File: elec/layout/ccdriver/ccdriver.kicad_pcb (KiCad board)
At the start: 2 copper layers, 25.4 x 14.8 mm, 31 parts, among them U1 ?, U2 ?, U3 ?, U4 ?, U5 ?, U6 ?, U7 ?

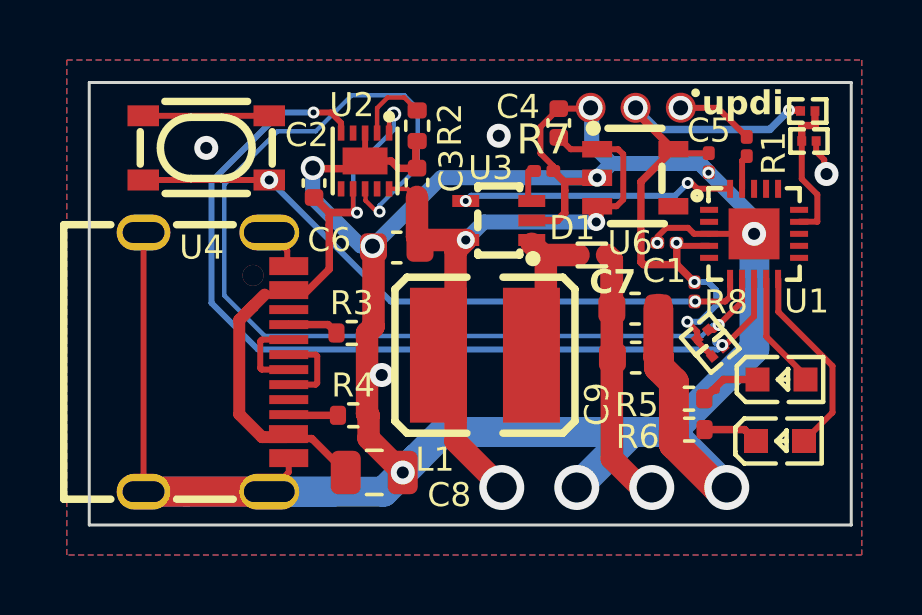
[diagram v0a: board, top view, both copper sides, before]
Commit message: fixed ground plane
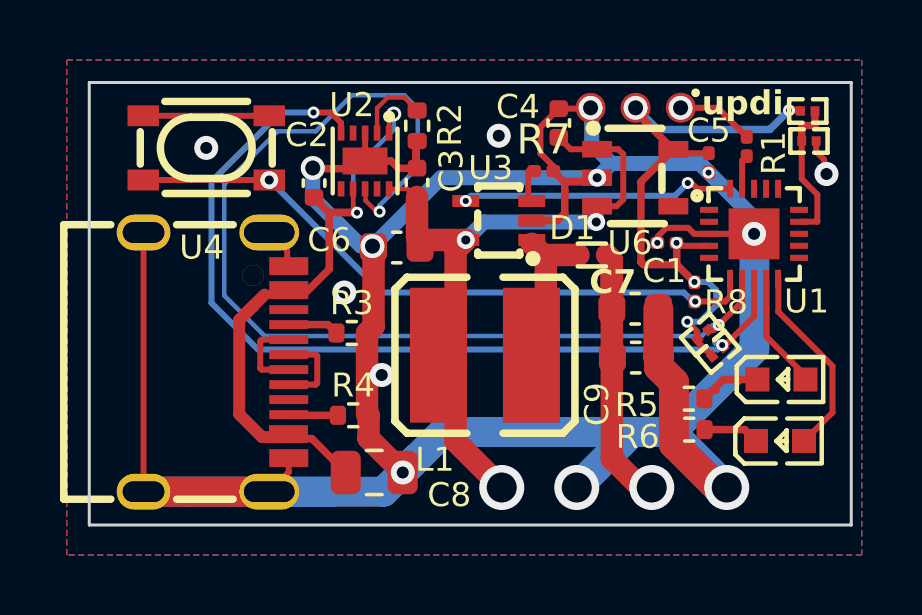
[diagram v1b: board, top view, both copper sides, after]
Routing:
- net gnd: vias 14 -> 15
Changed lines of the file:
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@@
 	)
 	(segment
-		(start 189.45 118.55)
-		(end 179.3 118.55)
+		(start 189.367893 118.55)
+		(end 189.067893 118.25)
 		(width 0.2)
 		(layer "B.Cu")
@@
 	)
 	(segment
-		(start 179.3 118.55)
+		(start 179 118.25)
 		(end 175.25 114.5)
+		(width 0.2)
+		(layer "B.Cu")
+		(net 33)
+	)
+	(segment
+		(start 189.067893 118.25)
+		(end 179 118.25)
+		(width 0.2)
+		(layer "B.Cu")
+		(net 33)
+	)
+	(segment
+		(start 189.45 118.55)
+		(end 189.367893 118.55)
 		(width 0.2)
 		(layer "B.Cu")
@@
 		(size 0.8)
 		(drill 0.4)
+		(layers "F.Cu" "B.Cu")
+		(net 36)
+	)
+	(via
+		(at 177.75 118.25)
+		(size 0.8)
+		(drill 0.4)

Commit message: fixed maybe
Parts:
- added ?: , , F.Cu at (174.7, 123.6)
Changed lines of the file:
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@@
 		)
 	)
+	(footprint ""
+		(layer "F.Cu")
+		(at 174.71 123.58)
+		(property "Reference" ""
+			(at 0 0 0)
+			(layer "F.SilkS")
+			(effects
+				(font
+					(size 1.27 1.27)
+					(thickness 0.15)
+				)
+			)
+		)
+		(property "Value" ""
+			(at 0 0 0)
+			(layer "F.Fab")
+			(effects
+				(font
+					(size 1.27 1.27)
+					(thickness 0.15)
+				)
+			)
+		)
+		(property "Footprint" ""
+			(at 0 0 0)
+			(layer "F.Fab")
+			(hide yes)
+			(effects
+				(font
+					(size 1.27 1.27)
+					(thickness 0.15)
+				)
+			)
+		)
+		(property "Datasheet" ""
+			(at 0 0 0)
+			(layer "F.Fab")
+			(hide yes)
+			(effects
+				(font
+					(size 1.27 1.27)
+					(thickness 0.15)
+				)
+			)
+		)
+		(property "Description" ""
+			(at 0 0 0)
+			(layer "F.Fab")
+			(hide yes)
+			(effects
+				(font
+					(size 1.27 1.27)
+					(thickness 0.15)
+				)
+			)
+		)
+		(pad "" thru_hole circle
+			(at 0 0 270)
+			(size 0.7 0.7)
+			(drill 0.7)
+			(layers "*.Cu" "*.Mask")
+			(remove_unused_layers no)
+		)
+	)
 	(footprint "lib:C0201"
 		(layer "F.Cu")
@@
 			(pintype "stereo")
 		)
-		(model "/Users/narayanpowderly/Documents/atopile-workspace/blinky/.ato/modules/generics/elec/footprints/footprints.3dshapes/KEY-SMD_4P-L4.2-W3.2-H2.5-LS4.6-P2.2.wrl"
-			(offset
-				(xyz 0 -0 -0)
-			)
-			(scale
-				(xyz 1 1 1)
-			)
-			(rotate
-				(xyz 0 0 0)
-			)
-		)
 		(model "/home/lucy/Documents/atopile/uv-lamp/elec/src/generics/elec/footprints/footprints.3dshapes/KEY-SMD_4P-L4.2-W3.2-H2.5-LS4.6-P2.2.wrl"
 			(offset
@@
 			(pintype "stereo")
 		)
-		(model "/home/lucy/Documents/atopile/uv-lamp/elec/footprints/footprints.3dshapes/R0201_L0.6-W0.3-H0.3.wrl"
+		(model "/home/lucy/Documents/atopile/uv-lamp/elec/footprints/footprints.3dshapes/R0201_L0.6-W0.3-H0.3.step"
 			(offset
-				(xyz 0 -0 0)
+				(xyz 0 0 0)
 			)
 			(scale
@@
 		)
 	)
+	(group "usbc"
+		(members "0eba9e7e-9961-4430-bbc1-5fd2411052b9" "27a406e7-5e6e-4e30-97f1-307150997ea0"
+			"3cdb961b-0bb8-440d-87d0-63ed2485c148" "b149c854-9efb-48dd-a56e-2ed54e9f511d"
+		)
+	)
 	(group "bms"
 		(members "065813e5-c59f-40af-b694-4187faafd556" "090c250a-4bac-4b26-8385-9bee2f677c20"
@@
 			"d1912bbc-6584-4f6d-acbb-54d09b2e1849" "d4cc0b65-6a06-457f-bd0b-a70b7c8b1314"
 			"dde265e8-a81b-4e2f-8976-f1b2dd06b422" "e151fd66-8c8f-4e4b-a593-4c329eb5e57d"
-			"e15e8724-5225-4e31-9fd4-3d45aa813b05" "e299cd47-7bbd-4857-b26b-47334b1d9110"
-			"e870fe11-1c06-4db3-8bcc-d51fd6cee0e8" "e8b14bf2-3dfa-4f08-bfec-ab5f514f2201"
-			"e93e4ba7-0f7c-431d-9441-7e8d030ead60" "ef90a151-1f2f-46e1-9d48-bcddb10059bc"
-			"f62ab995-2f69-45c6-8b5e-7bb48851861e"
-		)
-	)
-	(group "usbc"
-		(members "0eba9e7e-9961-4430-bbc1-5fd2411052b9" "14b0757e-5a05-43cc-9dcb-e36f415582b7"
-			"1e5da911-d3d1-48b5-8e10-88d5e9b217c3" "2cac2d1e-38f8-4df2-9768-7ddb98c64f72"
-			"35eff634-b1c2-4418-b5fb-d841a103856d" "3cdb961b-0bb8-440d-87d0-63ed2485c148"
-			"53fc9f3b-3ce1-473a-a470-b0eb2fb783e3" "5f0b0757-f060-49fe-a368-c9962dd733f3"
-			"604e9768-d2a7-48e0-8cd7-c7f58274474f" "715ff7f1-b2f5-456b-9b10-10c1a9070828"
-			"b149c854-9efb-48dd-a56e-2ed54e9f511d" "eb731c1c-37ec-4fc3-863e-153d89de7e77"
+			"e15e8724-5225-4e31-9fd4-3d45aa813b05" "e870fe11-1c06-4db3-8bcc-d51fd6cee0e8"
+			"e8b14bf2-3dfa-4f08-bfec-ab5f514f2201" "e93e4ba7-0f7c-431d-9441-7e8d030ead60"
+			"ef90a151-1f2f-46e1-9d48-bcddb10059bc" "f62ab995-2f69-45c6-8b5e-7bb48851861e"
 		)
 	)

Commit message: fixed maybe
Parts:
- removed ?: , 
- R7: value 100mW 300mΩ Chip Splitter 0ppm/℃~+300ppm/℃ ±1% 0201 Current Sense Resistors / Shunt Resistors ROHS -> 62.5mW Thick Film Resistors 50V ±1% 300mΩ 0402 Chip Resistor - Surface Mount ROHS; footprint lib:R0201 -> lib:R0402
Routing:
- net temp: track 4.92 -> 8.82 mm
- net uc.ic-vcc-1: track 3.90 -> 0.00 mm
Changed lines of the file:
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@@
 	(net 35 "full_led.resistor-cathode")
 	(net 36 "gnd")
-	(net 37 "uc.ic-vcc-2")
-	(net 38 "uc.ic-vcc-1")
-	(net 39 "temp")
+	(net 37 "temp")
+	(net 38 "uc.ic-vcc-2")
 	(footprint "lib:IND-SMD_L4.5-W4.0"
 		(layer "F.Cu")
@@
 			(size 0.8 0.8)
 			(layers "F.Cu" "F.Paste" "F.Mask")
-			(net 38 "uc.ic-vcc-1")
+			(net 37 "uc.ic-vcc-1")
 			(pintype "stereo")
 		)
@@
 		)
 	)
-	(footprint "lib:R0201"
+	(footprint "lib:R0402"
 		(layer "F.Cu")
 		(at 184.4 114.2)
-		(descr "Resistor SMD 0201 (0603 Metric), square (rectangular) end terminal, IPC_7351 nominal, (Body size source: https://www.vishay.com/docs/20052/crcw0201e3.pdf), generated with kicad-footprint-generator")
+		(descr "Resistor SMD 0402 (1005 Metric), square (rectangular) end terminal, IPC_7351 nominal, (Body size source: IPC-SM-782 page 72, https://www.pcb-3d.com/wordpress/wp-content/uploads/ipc-sm-782a_amendment_1_and_2.pdf), generated with kicad-footprint-generator")
 		(tags "resistor")
 		(property "Reference" "R7"
-			(at 0 -1.05 0)
+			(at 0 -1.17 0)
 			(layer "F.SilkS")
 			(effects
@@
 			)
 		)
-		(property "Value" "100mW 300mΩ Chip Splitter 0ppm/℃~+300ppm/℃ ±1% 0201  Current Sense Resistors / Shunt Resistors ROHS"
-			(at 0 1.05 0)
+		(property "Value" "62.5mW Thick Film Resistors 50V ±1% 300mΩ 0402  Chip Resistor - Surface Mount ROHS"
+			(at 0 1.17 0)
 			(layer "F.Fab")
 			(effects
@@
 		(attr smd)
 		(fp_line
-			(start -0.7 -0.35)
-			(end 0.7 -0.35)
+			(start -0.153641 -0.38)
+			(end 0.153641 -0.38)
+			(stroke
+				(width 0.12)
+				(type solid)
+			)
+			(layer "F.SilkS")
+		)
+		(fp_line
+			(start -0.153641 0.38)
+			(end 0.153641 0.38)
+			(stroke
+				(width 0.12)
+				(type solid)
+			)
+			(layer "F.SilkS")
+		)
+		(fp_line
+			(start -0.93 -0.47)
+			(end 0.93 -0.47)
 			(stroke
 				(width 0.05)
@@
 		)
 		(fp_line
-			(start -0.7 0.35)
-			(end -0.7 -0.35)
+			(start -0.93 0.47)
+			(end -0.93 -0.47)
 			(stroke
 				(width 0.05)
@@
 		)
 		(fp_line
-			(start 0.7 -0.35)
-			(end 0.7 0.35)
+			(start 0.93 -0.47)
+			(end 0.93 0.47)
 			(stroke
 				(width 0.05)
@@
 		)
 		(fp_line
-			(start 0.7 0.35)
-			(end -0.7 0.35)
+			(start 0.93 0.47)
+			(end -0.93 0.47)
 			(stroke
 				(width 0.05)
@@
 		)
 		(fp_line
-			(start -0.3 -0.15)
-			(end 0.3 -0.15)
+			(start -0.525 -0.27)
+			(end 0.525 -0.27)
 			(stroke
 				(width 0.1)
@@
 		)
 		(fp_line
-			(start -0.3 0.15)
-			(end -0.3 -0.15)
+			(start -0.525 0.27)
+			(end -0.525 -0.27)
 			(stroke
 				(width 0.1)
@@
 		)
 		(fp_line
-			(start 0.3 -0.15)
-			(end 0.3 0.15)
+			(start 0.525 -0.27)
+			(end 0.525 0.27)
 			(stroke
 				(width 0.1)
@@
 		)
 		(fp_line
-			(start 0.3 0.15)
-			(end -0.3 0.15)
+			(start 0.525 0.27)
+			(end -0.525 0.27)
 			(stroke
 				(width 0.1)
@@
 		)
 		(fp_text user "${REFERENCE}"
-			(at 0 -0.68 0)
+			(at 0 0 0)
 			(layer "F.Fab")
 			(effects
 				(font
-					(size 0.25 0.25)
+					(size 0.26 0.26)
 					(thickness 0.04)
 				)
 			)
 		)
-		(pad "" smd roundrect
-			(at -0.345 0)
-			(size 0.318 0.36)
-			(layers "F.Paste")
-			(roundrect_rratio 0.25)
-		)
-		(pad "" smd roundrect
-			(at 0.345 0)
-			(size 0.318 0.36)
-			(layers "F.Paste")
-			(roundrect_rratio 0.25)
-		)
 		(pad "1" smd roundrect
-			(at -0.32 0)
-			(size 0.46 0.4)
-			(layers "F.Cu" "F.Mask")
+			(at -0.51 0)
+			(size 0.54 0.64)
+			(layers "F.Cu" "F.Paste" "F.Mask")
 			(roundrect_rratio 0.25)
 			(net 18 "fb")
@@
 		)
 		(pad "2" smd roundrect
-			(at 0.32 0)
-			(size 0.46 0.4)
-			(layers "F.Cu" "F.Mask")
+			(at 0.51 0)
+			(size 0.54 0.64)
+			(layers "F.Cu" "F.Paste" "F.Mask")
 			(roundrect_rratio 0.25)
 			(net 36 "gnd")
 			(pintype "stereo")
 		)
-		(model "${KICAD6_3DMODEL_DIR}/Resistor_SMD.3dshapes/R_0201_0603Metric.wrl"
+		(model "${KICAD6_3DMODEL_DIR}/Resistor_SMD.3dshapes/R_0402_1005Metric.wrl"
 			(offset
 				(xyz 0 0 0)
@@
 		)
 	)
-	(footprint ""
-		(layer "F.Cu")
-		(at 174.71 123.58)
-		(property "Reference" ""
-			(at 0 0 0)
-			(layer "F.SilkS")
-			(effects
-				(font
-					(size 1.27 1.27)
-					(thickness 0.15)
-				)
-			)
-		)
-		(property "Value" ""
-			(at 0 0 0)
-			(layer "F.Fab")
-			(effects
-				(font
-					(size 1.27 1.27)
-					(thickness 0.15)
-				)
-			)
-		)
-		(property "Footprint" ""
-			(at 0 0 0)
-			(layer "F.Fab")
-			(hide yes)
-			(effects
-				(font
-					(size 1.27 1.27)
-					(thickness 0.15)
-				)
-			)
-		)
-		(property "Datasheet" ""
-			(at 0 0 0)
-			(layer "F.Fab")
-			(hide yes)
-			(effects
-				(font
-					(size 1.27 1.27)
-					(thickness 0.15)
-				)
-			)
-		)
-		(property "Description" ""
-			(at 0 0 0)
-			(layer "F.Fab")
-			(hide yes)
-			(effects
-				(font
-					(size 1.27 1.27)
-					(thickness 0.15)
-				)
-			)
-		)
-		(pad "" thru_hole circle
-			(at 0 0 270)
-			(size 0.7 0.7)
-			(drill 0.7)
-			(layers "*.Cu" "*.Mask")
-			(remove_unused_layers no)
-		)
-	)
 	(footprint "lib:C0201"
 		(layer "F.Cu")
@@
 			(size 0.3 0.32)
 			(layers "F.Cu" "F.Paste" "F.Mask")
-			(net 39 "temp")
+			(net 37 "temp")
 			(pintype "stereo")
 		)
@@
 			(size 0.3 0.32)
 			(layers "F.Cu" "F.Paste" "F.Mask")
-			(net 39 "temp")
+			(net 37 "temp")
 			(pintype "stereo")
 		)
@@
 			(size 0.8 0.8)
 			(layers "F.Cu" "F.Paste" "F.Mask")
-			(net 37 "uc.ic-vcc-2")
+			(net 38 "uc.ic-vcc-2")
 			(pintype "stereo")
 		)
@@
 			(size 0.2 0.6)
 			(layers "F.Cu" "F.Paste" "F.Mask")
-			(net 38 "uc.ic-vcc-1")
+			(net 37 "uc.ic-vcc-1")
 			(pintype "stereo")
 		)
@@
 			(size 0.2 0.6)
 			(layers "F.Cu" "F.Paste" "F.Mask")
-			(net 37 "uc.ic-vcc-2")
+			(net 38 "uc.ic-vcc-2")
 			(pintype "stereo")
 		)
@@
 			(size 0.6 0.2)
 			(layers "F.Cu" "F.Paste" "F.Mask")
-			(net 39 "temp")
+			(net 37 "temp")
 			(pintype "stereo")
 		)
@@
 	)
 	(segment
-		(start 194.025 122.25)
-		(end 194.025 120.7)
-		(width 0.2)
+		(start 193.04 112.685)
+		(end 193.435 112.685)
+		(width 0.25)
 		(layer "F.Cu")
 		(net 37)
 	)
 	(segment
-		(start 193.075 123.2)
-		(end 194.025 122.25)
+		(start 193.125 121.025)
+		(end 193.125 121.15)
 		(width 0.2)
 		(layer "F.Cu")
@@
 	)
 	(segment
-		(start 192.22 118.895)
-		(end 192.22 117.79)
-		(width 0.2)
+		(start 193 113.2)
+		(end 193 112.725)
+		(width 0.25)
 		(layer "F.Cu")
 		(net 37)
 	)
 	(segment
-		(start 194.025 120.7)
-		(end 192.22 118.895)
+		(start 193.52 114.98495)
+		(end 193 114.46495)
 		(width 0.2)
 		(layer "F.Cu")
@@
 	)
 	(segment
-		(start 193.125 121.025)
-		(end 193.125 121.15)
-		(width 0.2)
+		(start 193.435 112.685)
+		(end 193.44 112.68)
+		(width 0.25)
 		(layer "F.Cu")
-		(net 38)
+		(net 37)
 	)
 	(segment
-		(start 191.82 117.79)
-		(end 191.82 119.72)
+		(start 193 114.46495)
+		(end 193 113.2)
 		(width 0.2)
 		(layer "F.Cu")
-		(net 38)
+		(net 37)
 	)
 	(segment
-		(start 191.82 119.72)
-		(end 193.125 121.025)
+		(start 192.92 115.89)
+		(end 193.52 115.89)
 		(width 0.2)
 		(layer "F.Cu")
-		(net 38)
+		(net 37)
 	)
 	(segment
-		(start 193.04 112.685)
-		(end 193.435 112.685)
-		(width 0.25)
+		(start 191.82 117.79)
+		(end 191.82 119.72)
+		(width 0.2)
 		(layer "F.Cu")
-		(net 39)
+		(net 37)
 	)
 	(segment
-		(start 193 113.2)
-		(end 193 112.725)
+		(start 193 112.725)
+		(end 193.04 112.685)
 		(width 0.25)
 		(layer "F.Cu")
-		(net 39)
+		(net 37)
 	)
 	(segment
-		(start 193.52 114.98495)
-		(end 193 114.46495)
+		(start 191.82 119.72)
+		(end 193.125 121.025)
 		(width 0.2)
 		(layer "F.Cu")
-		(net 39)
+		(net 37)
 	)
 	(segment
-		(start 193.435 112.685)
-		(end 193.44 112.68)
-		(width 0.25)
+		(start 193.52 115.89)
+		(end 193.52 114.98495)
+		(width 0.2)
 		(layer "F.Cu")
-		(net 39)
+		(net 37)
 	)
 	(segment
-		(start 193 114.46495)
-		(end 193 113.2)
-		(width 0.2)
+		(start 193.44 112.68)
+		(end 193.44 112.2)
+		(width 0.25)
 		(layer "F.Cu")
-		(net 39)
+		(net 37)
 	)
 	(segment
-		(start 192.92 115.89)
-		(end 193.52 115.89)
+		(start 194.025 122.25)
+		(end 194.025 120.7)
 		(width 0.2)
 		(layer "F.Cu")
-		(net 39)
+		(net 38)
 	)
 	(segment
-		(start 193 112.725)
-		(end 193.04 112.685)
-		(width 0.25)
+		(start 193.075 123.2)
+		(end 194.025 122.25)
+		(width 0.2)
 		(layer "F.Cu")
-		(net 39)
+		(net 38)
 	)
 	(segment
-		(start 193.52 115.89)
-		(end 193.52 114.98495)
+		(start 192.22 118.895)
+		(end 192.22 117.79)
 		(width 0.2)
 		(layer "F.Cu")
-		(net 39)
+		(net 38)
 	)
 	(segment
-		(start 193.44 112.68)
-		(end 193.44 112.2)
-		(width 0.25)
+		(start 194.025 120.7)
+		(end 192.22 118.895)
+		(width 0.2)
 		(layer "F.Cu")
-		(net 39)
+		(net 38)
 	)
 	(zone
@@
 	)
 	(group "usbc"
-		(members "0eba9e7e-9961-4430-bbc1-5fd2411052b9" "27a406e7-5e6e-4e30-97f1-307150997ea0"
-			"3cdb961b-0bb8-440d-87d0-63ed2485c148" "b149c854-9efb-48dd-a56e-2ed54e9f511d"
+		(members "0eba9e7e-9961-4430-bbc1-5fd2411052b9" "3cdb961b-0bb8-440d-87d0-63ed2485c148"
+			"b149c854-9efb-48dd-a56e-2ed54e9f511d"
 		)
 	)

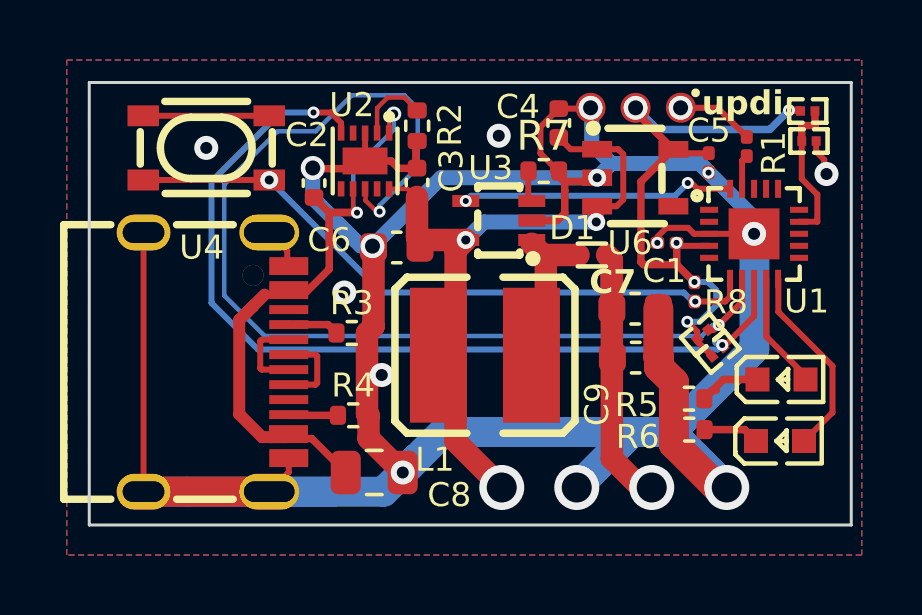
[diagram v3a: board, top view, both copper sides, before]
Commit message: fixed usbc and vias
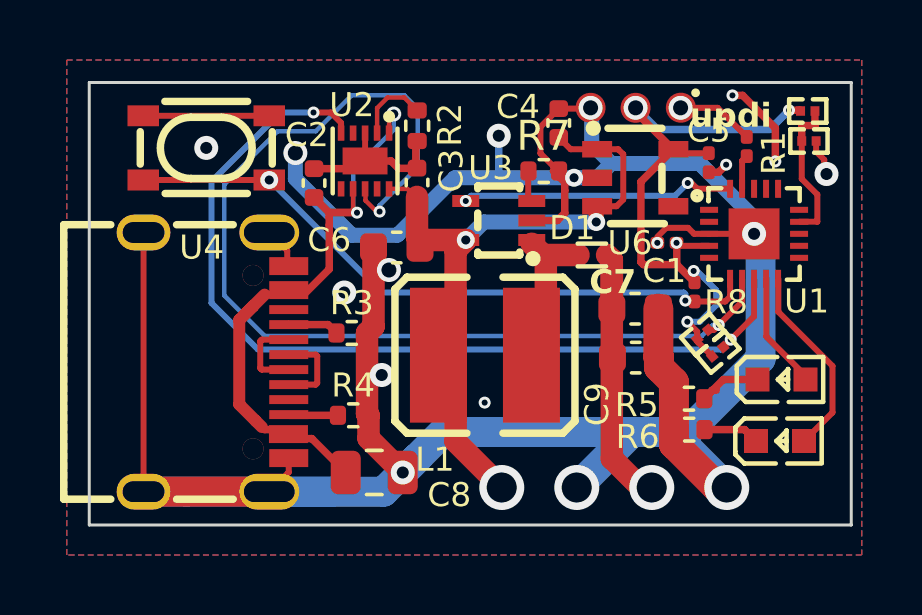
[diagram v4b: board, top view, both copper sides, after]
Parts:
- added ?: , , F.Cu at (174.7, 123.5)
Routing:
- net gnd: track 113.0 -> 119.1 mm, vias 15 -> 18
- net temp: track 8.82 -> 4.92 mm
- net uc.ic-vcc-1: track 0.00 -> 3.90 mm
